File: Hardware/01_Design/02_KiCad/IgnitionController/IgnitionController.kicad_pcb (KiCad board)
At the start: 2 copper layers, 179 parts, among them J1 770669-1, Q1 SS8050, Q10 IRF540N, Q11 IRF540N, Q2 DMP6050SSD, Q3 DMP6050SSD, Q4 RSJ250P10, Q5 BC856, Q6 IRF9Z34NSPbF, Q7 SS8050, Q8 IRF540N, Q9 IRF540N, U1 ATmega328PB-A, U10 TLV2372, U11 TLV2372, U12 STM32F407VGTx, U14 AT24CS01-SSHM, U15 MCP2557FD-xSN, U19 IXDN602, U2 4N35, U20 IXDN602, U23 4N35, U24 4N35, U25 TXS0104EPW, U3 LM2575-3.3BU, U4 LM2575-5.0BU, U5 4N35, U6 4N35, U7 4N35, U8 TXS0104EPW, U9 LM2575-5.0BU, Y1 16MHz, Y2 32.768kHz, Y3 8MHz

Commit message: Initial routing of Power supply
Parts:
- removed C10, C8: UCL1V331MNL1GS, Capacitor_SMD:CP_Elec_10x12.5
- removed C6: UCL1V101MNL1GS, Capacitor_SMD:CP_Elec_8x11.9
- removed D11: RED, LED_SMD:LED_0805_2012Metric_Pad1.15x1.40mm_HandSolder
- removed D9: SS14, Diode_SMD:D_SMA
- removed L3, L4: L_Iron, Inductor_SMD:L_7.3x7.3_H3.5
- removed R11: 470R, Resistor_SMD:R_0805_2012Metric_Pad1.20x1.40mm_HandSolder
- added C43: 1u, Capacitor_SMD:C_0603_1608Metric_Pad1.08x0.95mm_HandSolder, F.Cu at (169.6, 36.0)
- added C44: 0.1u, Capacitor_SMD:C_0603_1608Metric_Pad1.08x0.95mm_HandSolder, F.Cu at (169.6, 38.5)
- added C45: 100n, Capacitor_SMD:C_0603_1608Metric_Pad1.08x0.95mm_HandSolder, F.Cu at (169.6, 41.0)
- added C46: 100n, Capacitor_SMD:C_0603_1608Metric_Pad1.08x0.95mm_HandSolder, F.Cu at (169.6, 43.5)
- added C47: 0.1u, Capacitor_SMD:C_0603_1608Metric_Pad1.08x0.95mm_HandSolder, F.Cu at (174.0, 20.9)
- added C48: 1u, Capacitor_SMD:C_0603_1608Metric_Pad1.08x0.95mm_HandSolder, F.Cu at (174.0, 23.4)
- added C49: 1u, Capacitor_SMD:C_0603_1608Metric_Pad1.08x0.95mm_HandSolder, F.Cu at (174.0, 26.0)
- added C50: 0.1u, Capacitor_SMD:C_0603_1608Metric_Pad1.08x0.95mm_HandSolder, F.Cu at (174.0, 28.5)
- added C51: 0.1u, Capacitor_SMD:C_0603_1608Metric_Pad1.08x0.95mm_HandSolder, F.Cu at (174.0, 31.0)
- added C52: UCL1V101MNL1GS, Capacitor_SMD:CP_Elec_8x11.9, F.Cu at (76.7, 98.0)
- added C53: UCL0J331MCL1GS, Capacitor_SMD:CP_Elec_6.3x7.7, F.Cu at (76.4, 108.4)
- added C54: UCL0J331MCL1GS, Capacitor_SMD:CP_Elec_6.3x7.7, F.Cu at (76.5, 85.6)
- added D23: SM6T100A, Diode_SMD:D_SMB, F.Cu at (271.6, 78.0)
- added D24: SM6T100A, Diode_SMD:D_SMB, F.Cu at (271.6, 83.6)
- added D25: SM6T100A, Diode_SMD:D_SMB, F.Cu at (271.6, 89.1)
- added D26: SM6T100A, Diode_SMD:D_SMB, F.Cu at (271.6, 94.7)
- added D27: RED, LED_SMD:LED_1206_3216Metric_Pad1.42x1.75mm_HandSolder, F.Cu at (206.0, 62.7)
- added D28: RED, LED_SMD:LED_1206_3216Metric_Pad1.42x1.75mm_HandSolder, F.Cu at (206.0, 66.1)
- added D29: RED, LED_SMD:LED_1206_3216Metric_Pad1.42x1.75mm_HandSolder, F.Cu at (206.0, 69.5)
- added D30: RED, LED_SMD:LED_1206_3216Metric_Pad1.42x1.75mm_HandSolder, F.Cu at (206.0, 72.9)
- added D31: SS14, Diode_SMD:D_SMA, B.Cu at (90.6, 107.6)
- added D32: RED, LED_SMD:LED_0805_2012Metric_Pad1.15x1.40mm_HandSolder, F.Cu at (100.8, 98.2)
- added J2: Conn_02x03_Odd_Even, Connector_IDC:IDC-Header_2x03_P2.54mm_Vertical, F.Cu at (223.2, 94.5)
- added J3: FTSH-105-01-L-DV-A, FTSH-105-01-L-DV-A:FTSH-105-XX-YYY-DV-A, F.Cu at (234.8, 93.3)
- added L6: SRR1280-331K, Inductor_SMD:L_Bourns_SRR1260, F.Cu at (91.0, 103.4)
- added L7: SRR1280-331K, Inductor_SMD:L_Bourns_SRR1260, F.Cu at (91.0, 87.6)
- added Q12: IRF540N, Package_TO_SOT_THT:TO-220-3_Vertical, F.Cu at (259.0, 79.2)
- added Q13: IRF540N, Package_TO_SOT_THT:TO-220-3_Vertical, F.Cu at (259.0, 85.1)
- added Q14: IRF540N, Package_TO_SOT_THT:TO-220-3_Vertical, F.Cu at (259.0, 91.1)
- added Q15: IRF540N, Package_TO_SOT_THT:TO-220-3_Vertical, F.Cu at (259.0, 97.1)
- added R58: 120R, Resistor_SMD:R_0603_1608Metric_Pad0.98x0.95mm_HandSolder, F.Cu at (178.3, 36.0)
- added R66: 100R, Resistor_SMD:R_0603_1608Metric_Pad0.98x0.95mm_HandSolder, F.Cu at (277.9, 76.5)
- added R67: 100R, Resistor_SMD:R_0603_1608Metric_Pad0.98x0.95mm_HandSolder, F.Cu at (277.9, 79.0)
- added R68: 100R, Resistor_SMD:R_0603_1608Metric_Pad0.98x0.95mm_HandSolder, F.Cu at (277.9, 81.5)
- added R69: 100R, Resistor_SMD:R_0603_1608Metric_Pad0.98x0.95mm_HandSolder, F.Cu at (277.9, 84.0)
- added R70: 7K, Resistor_SMD:R_0603_1608Metric_Pad0.98x0.95mm_HandSolder, F.Cu at (182.7, 28.5)
- added R71: 10K, Resistor_SMD:R_0603_1608Metric_Pad0.98x0.95mm_HandSolder, F.Cu at (182.7, 31.0)
- added R72: 8.2K, Resistor_SMD:R_0603_1608Metric_Pad0.98x0.95mm_HandSolder, F.Cu at (182.7, 33.5)
- added R73: 8.2K, Resistor_SMD:R_0603_1608Metric_Pad0.98x0.95mm_HandSolder, F.Cu at (182.7, 36.0)
- added R74: 7K, Resistor_SMD:R_0603_1608Metric_Pad0.98x0.95mm_HandSolder, F.Cu at (182.7, 38.5)
- added R75: 10K, Resistor_SMD:R_0603_1608Metric_Pad0.98x0.95mm_HandSolder, F.Cu at (182.7, 41.0)
- added R76: 10K, Resistor_SMD:R_0603_1608Metric_Pad0.98x0.95mm_HandSolder, F.Cu at (182.7, 43.5)
- added R77: 100R, Resistor_SMD:R_0603_1608Metric_Pad0.98x0.95mm_HandSolder, F.Cu at (189.0, 23.2)
- added R78: 100R, Resistor_SMD:R_0603_1608Metric_Pad0.98x0.95mm_HandSolder, F.Cu at (189.0, 25.7)
- added R79: 100R, Resistor_SMD:R_0603_1608Metric_Pad0.98x0.95mm_HandSolder, F.Cu at (189.0, 28.2)
- added R80: 100R, Resistor_SMD:R_0603_1608Metric_Pad0.98x0.95mm_HandSolder, F.Cu at (189.0, 30.7)
- added R81: 2K, Resistor_SMD:R_0603_1608Metric_Pad0.98x0.95mm_HandSolder, F.Cu at (189.0, 33.2)
- added R82: 2K, Resistor_SMD:R_0603_1608Metric_Pad0.98x0.95mm_HandSolder, F.Cu at (189.0, 35.7)
- added R83: 2K, Resistor_SMD:R_0603_1608Metric_Pad0.98x0.95mm_HandSolder, F.Cu at (189.0, 38.2)
- added R84: 2K, Resistor_SMD:R_0603_1608Metric_Pad0.98x0.95mm_HandSolder, F.Cu at (189.0, 40.7)
- added R85: 470R, Resistor_SMD:R_0603_1608Metric_Pad0.98x0.95mm_HandSolder, F.Cu at (104.3, 101.5)
- added U13: TLV2372, Package_SO:SOIC-8_5.3x6.2mm_P1.27mm, F.Cu at (208.2, 78.5)
- added U16: MAX232, Package_SO:SOIC-16_3.9x9.9mm_P1.27mm, F.Cu at (207.2, 55.3)
- added U21: IXDN602, Package_SO:SO-8_3.9x4.9mm_P1.27mm, F.Cu at (198.7, 79.1)
- added U22: IXDN602, Package_SO:SO-8_3.9x4.9mm_P1.27mm, F.Cu at (210.9, 101.7)
- C1, C13, C14, C15, C16, C17, C18, C19, C2, C20, C21, C22, C23, C24, C25, C26, C27, C28, C29, C3, C30, C31, C32, C33, C34, C35, C36, C37, C38, C39, C4, C40, C41, C42, C5, C7: footprint Capacitor_SMD:C_0805_2012Metric_Pad1.18x1.45mm_HandSolder -> Capacitor_SMD:C_0603_1608Metric_Pad1.08x0.95mm_HandSolder
- C12: value UCL1V331MNL1GS -> UCL0J331MCL1GS; footprint Capacitor_SMD:CP_Elec_10x12.5 -> Capacitor_SMD:CP_Elec_6.3x7.7
- D12, D13, D15, D8, Q5, U3, U4, U9: moved to B.Cu
- L5: value L_Iron -> SRR1280-331K; footprint Inductor_SMD:L_7.3x7.3_H3.5 -> Inductor_SMD:L_Bourns_SRR1260
- Q4: value RSJ250P10 -> RSJ250P10FRATL; footprint Package_TO_SOT_SMD:TO-263-2 -> Library:TO-263-2_Transistor; moved to B.Cu
- Q6: value IRF9Z34NSPbF -> 942-IRF9Z34NSPBF; footprint Package_TO_SOT_SMD:TO-263-2 -> Library:TO-263-2_Transistor; moved to B.Cu
- R1, R10, R12, R13, R14, R2, R3, R4, R40, R41, R42, R43, R44, R45, R46, R47, R48, R49, R50, R51, R52, R53, R54, R55, R56, R57, R59, R60, R61, R62, R63, R64, R65, R8: footprint Resistor_SMD:R_0805_2012Metric_Pad1.20x1.40mm_HandSolder -> Resistor_SMD:R_0603_1608Metric_Pad0.98x0.95mm_HandSolder
- R15, R16, R17, R18, R19, R20, R21, R22, R24, R25, R26, R27, R28, R29, R30, R31, R32, R33, R34, R35, R36, R37, R38, R39, R5, R6, R7: footprint Resistor_SMD:R_0805_2012Metric_Pad1.20x1.40mm_HandSolder -> Resistor_SMD:R_0603_1608Metric_Pad0.98x0.95mm_HandSolder; moved to F.Cu
- R23, R9: footprint Resistor_SMD:R_0815_2038Metric_Pad1.20x4.05mm_HandSolder -> Resistor_SMD:R_0603_1608Metric_Pad0.98x0.95mm_HandSolder
- U23, U24: moved to F.Cu
- moved U11 163.7 mm to (251.8, 23.7), turned to 0 degrees
- moved U10 162.9 mm to (251.8, 16.0), turned to 0 degrees
- moved U1 155.7 mm to (262.8, 30.3)
- moved R9 151.2 mm to (121.5, 116.4), turned to 90 degrees
- moved D8 151.1 mm to (98.5, 123.2)
- moved R33 145.8 mm to (244.4, 18.4), turned to 0 degrees
- moved R32 145.6 mm to (244.4, 15.8), turned to 0 degrees
- moved D16 145.4 mm to (100.8, 114.7)
- moved R31 145.3 mm to (244.4, 13.3), turned to 0 degrees
- moved D10 144.6 mm to (113.9, 108.9), turned to -90 degrees
- moved Q5 143.5 mm to (103.1, 123.2), turned to 180 degrees
- moved D14 142.2 mm to (100.8, 83.0)
- moved C7 141.7 mm to (124.4, 120.9), turned to 90 degrees
- moved R39 141.7 mm to (244.4, 33.4), turned to 0 degrees
- moved R38 141.5 mm to (244.4, 30.9), turned to 0 degrees
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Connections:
- net Net-(U1-PB3) renamed PMIC_SPI_MOSI
- net Net-(U1-PB4) renamed PMIC_SPI_MISO
- net Net-(U1-PB5) renamed PMIC_SPI_SCK
- net Net-(U12-NRST) renamed MCU_NRST
- J1 pad 1: unconnected-(J1-Pad1) -> GND
- J1 pad 10: unconnected-(J1-Pad10) -> INJ_FUEL_3
- J1 pad 11: unconnected-(J1-Pad11) -> MAP_SENSOR_SIGNAL
- J1 pad 12: unconnected-(J1-Pad12) -> TPS_SIGNAL
- J1 pad 13: unconnected-(J1-Pad13) -> COOLANT_TEMP_ADC_SIGNAL
- J1 pad 14: unconnected-(J1-Pad14) -> VSEN
- J1 pad 15: unconnected-(J1-Pad15) -> GND
- J1 pad 16: unconnected-(J1-Pad16) -> SENSOR_2_SIGNAL
- J1 pad 17: unconnected-(J1-Pad17) -> CAN-L
- J1 pad 18: unconnected-(J1-Pad18) -> UART_TX
- J1 pad 19: unconnected-(J1-Pad19) -> GND
- J1 pad 2: unconnected-(J1-Pad2) -> +BATT
- J1 pad 20: unconnected-(J1-Pad20) -> IGN_COIL_2
- J1 pad 21: unconnected-(J1-Pad21) -> IGN_COIL_4
- J1 pad 22: unconnected-(J1-Pad22) -> INJ_FUEL_2
- J1 pad 23: unconnected-(J1-Pad23) -> INJ_FUEL_4
- J1 pad 3: unconnected-(J1-Pad3) -> KL15
- J1 pad 4: unconnected-(J1-Pad4) -> SENSOR_1_SIGNAL
- J1 pad 5: unconnected-(J1-Pad5) -> CAN-H
- J1 pad 6: unconnected-(J1-Pad6) -> UART_RX
- J1 pad 7: unconnected-(J1-Pad7) -> IGN_COIL_1
- J1 pad 8: unconnected-(J1-Pad8) -> IGN_COIL_3
- J1 pad 9: unconnected-(J1-Pad9) -> INJ_FUEL_1
- Q4 pad 1: Net-(Q4-D) -> Net-(D8-A)
- Q4 pad 2: Net-(D8-A) -> Net-(Q4-D)
- Q6 pad 1: VCC -> Net-(D12-A)
- Q6 pad 2: Net-(D12-A) -> VCC
- U1 pad 29: unconnected-(U1-~{RESET}/PC6-Pad29) -> PMIC_RESET
- U12 pad 15: unconnected-(U12-PC0-Pad15) -> TPS_ADC_SIGNAL
- U12 pad 16: unconnected-(U12-PC1-Pad16) -> MAP_SENSOR_ADC_SIGNAL
- U12 pad 17: unconnected-(U12-PC2-Pad17) -> COOLANT_TEMP_ADC_SIGNAL
- U12 pad 63: unconnected-(U12-PC6-Pad63) -> Cylinder1FuelOut_Pin
- U12 pad 64: unconnected-(U12-PC7-Pad64) -> Cylinder2FuelOut_Pin
- U12 pad 65: unconnected-(U12-PC8-Pad65) -> Cylinder3FuelOut_Pin
- U12 pad 66: unconnected-(U12-PC9-Pad66) -> Cylinder4FuelOut_Pin
- U15 pad 6: unconnected-(U15-CANL-Pad6) -> CAN-L
- U15 pad 7: unconnected-(U15-CANH-Pad7) -> CAN-H
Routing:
- net GND: track 0.00 -> 249.2 mm, vias 0 -> 14
- net VCC: track 0.00 -> 84.0 mm, vias 0 -> 6
- net Net-(D12-A): track 0.00 -> 48.9 mm, vias 0 -> 4
- net Net-(D8-A): track 0.00 -> 46.5 mm, vias 0 -> 4
- net VPMIC: track 0.00 -> 46.2 mm, vias 0 -> 4
- net VSEN: track 0.00 -> 44.0 mm, vias 0 -> 3
- net Net-(Q4-D): track 0.00 -> 39.6 mm, vias 0 -> 3
- net Net-(D12-K): track 0.00 -> 35.9 mm, vias 0 -> 2
- net VMCU: track 0.00 -> 35.6 mm, vias 0 -> 3
- net Net-(D10-K): track 0.00 -> 22.0 mm, vias 0 -> 2
- net Net-(D13-K): track 0.00 -> 19.6 mm, vias 0 -> 3
- net Net-(D31-K): track 0.00 -> 13.9 mm, vias 0 -> 1
- net Net-(D15-K): track 0.00 -> 13.7 mm, vias 0 -> 1
- net Net-(D10-A): track 0.00 -> 10.2 mm
- net +BATT: track 0.00 -> 6.74 mm
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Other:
- copper layers 2 -> 4
- rule pad_to_mask_clearance: 0 -> 0.04
- board text added: "Layers: Top - Input Signals Layer 1 - Ground Layer 2 - Power Bottom - Output Signals"

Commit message: Added Crystal to PMIC
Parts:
- added R86: 10k, Resistor_SMD:R_0603_1608Metric_Pad0.98x0.95mm_HandSolder, F.Cu at (128.6, 85.5)
- added Y4: NX2016SA-16MHZ-EXS00A-CS07826, Library:NX2016SA16MHZEXS00ACS07826, F.Cu at (114.1, 94.1)
- Q2, Q3, R24, R25, R26, R27, R29, R30, R31, R32: moved to B.Cu
- U2, U5, U6, U7: moved to F.Cu
- moved Q3 176.5 mm to (76.7, 67.0), turned to 180 degrees
- moved Q2 176.4 mm to (76.7, 59.6), turned to 180 degrees
- moved R31 161.7 mm to (123.8, 121.1), turned to -90 degrees
- moved R35 159.8 mm to (89.7, 63.8)
- moved R36 158.1 mm to (89.6, 58.1)
- moved R38 157.4 mm to (89.6, 59.6)
- moved R37 157.3 mm to (89.6, 56.6)
- moved R32 155.9 mm to (129.4, 121.1), turned to -90 degrees
- moved U10 153.3 mm to (137.6, 118.3), turned to 180 degrees
- moved U1 151.7 mm to (124.7, 93.0)
- moved R19 149.8 mm to (89.7, 61.7)
- moved R18 148.4 mm to (89.7, 52.6)
- moved R17 147.4 mm to (89.7, 43.3)
- moved R16 146.6 mm to (89.7, 34.1)
- moved R30 143.4 mm to (126.5, 121.1), turned to -90 degrees
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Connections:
- C14 pad 1: GND -> Net-(U1-XTAL2/PB7)
- C14 pad 2: Net-(U1-XTAL1/PB6) -> GND
- C15 pad 2: Net-(U1-XTAL2/PB7) -> Net-(U1-XTAL1/PB6)
- C7 pad 1: Net-(Q4-D) -> +BATT_FUSE
- F1 pad 2: Net-(Q4-D) -> +BATT_FUSE
- Q2 pad 1: +BATT -> +BATT_FUSE
- Q2 pad 3: +BATT -> KL15
- Q3 pad 3: VMCU -> VMCU_OUT
- Q3 pad 5: VMCU_OUT -> VMCU
- Q3 pad 6: VMCU_OUT -> VMCU
- Q4 pad 2: Net-(Q4-D) -> +BATT_FUSE
- R24 pad 1: +BATT -> +BATT_FUSE
- U2 pad 5: +BATT -> +BATT_FUSE
- U5 pad 5: +BATT -> KL15
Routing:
- net GND: track 249.2 -> 527.9 mm, vias 14 -> 31
- net KL15: track 0.00 -> 184.7 mm, vias 0 -> 4
- net VPMIC: track 46.2 -> 228.4 mm, vias 4 -> 11
- net +BATT_FUSE: track 0.00 -> 165.9 mm, vias 0 -> 6
- net VMCU: track 35.6 -> 196.1 mm, vias 3 -> 12
- net VSEN: track 44.0 -> 141.9 mm, vias 3 -> 8
- net Net-(R5-Pad2): track 0.00 -> 68.4 mm
- net Net-(R6-Pad2): track 0.00 -> 60.3 mm
- net Net-(R7-Pad2): track 0.00 -> 51.9 mm
- net Net-(Q2A-G1): track 0.00 -> 46.8 mm, vias 0 -> 3
- net Net-(R15-Pad2): track 0.00 -> 43.9 mm
- net PMIC_SPI_MOSI: track 0.00 -> 42.7 mm, vias 0 -> 2
- net Net-(U11A-+): track 0.00 -> 42.3 mm, vias 0 -> 3
- net Net-(Q4-D): track 39.6 -> 0.00 mm, vias 3 -> 0
- net PMIC_SPI_MISO: track 0.00 -> 36.4 mm, vias 0 -> 2
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
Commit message: MCU HW Initial Layout
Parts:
- added Y1: FL0800011Q, Library:FL0800011Q, F.Cu at (99.6, 48.2)
- added Y3: XT1312HHRXX32K76E, Library:XT1312HHRXX32K76E, F.Cu at (105.0, 47.4)
- moved C32 134.8 mm to (97.4, 33.3), turned to 90 degrees
- moved C24 133.7 mm to (94.1, 33.3), turned to 90 degrees
- moved C33 133.7 mm to (99.0, 33.3), turned to 90 degrees
- moved R4 133.7 mm to (99.6, 56.0)
- moved D3 133.3 mm to (111.0, 66.2)
- moved C34 132.8 mm to (100.7, 33.3), turned to 90 degrees
- moved C25 132.7 mm to (95.7, 33.3), turned to 90 degrees
- moved C26 127.0 mm to (102.3, 33.3), turned to 90 degrees
- moved D4 126.9 mm to (117.1, 66.2)
- moved TP12 126.8 mm to (114.6, 62.1)
- moved C27 126.1 mm to (104.0, 33.3), turned to 90 degrees
- moved C28 125.3 mm to (105.6, 33.3), turned to 90 degrees
- moved C29 124.6 mm to (107.3, 33.3), turned to 90 degrees
- moved C30 123.9 mm to (108.9, 33.3), turned to 90 degrees
- moved C18 122.8 mm to (99.6, 44.6)
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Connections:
- C18 pad 1: GND -> Net-(U12-PH0)
- C18 pad 2: Net-(U12-PH0) -> GND
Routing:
- net GND: track 527.9 -> 687.2 mm, vias 31 -> 45
- net VMCU_OUT: track 11.7 -> 137.7 mm, vias 1 -> 10
- net Net-(U12-PH0): track 0.00 -> 19.1 mm
- net Net-(U12-PH1): track 0.00 -> 16.5 mm
- net MCU_NRST: track 0.00 -> 12.3 mm
- net Cylinder4Out_Pin: track 0.00 -> 8.56 mm
- net Net-(U12-PC14): track 0.00 -> 7.61 mm
- net Net-(U12-PC15): track 0.00 -> 6.87 mm
- net Net-(U12-BOOT0): track 0.00 -> 6.81 mm
- net Signal2_Pin: track 0.00 -> 6.33 mm
- net Signal1_Pin: track 0.00 -> 5.76 mm
- net Cylinder3Out_Pin: track 0.00 -> 5.13 mm
- net Net-(U12-PD15): track 0.00 -> 4.80 mm
- net Cylinder2Out_Pin: track 0.00 -> 4.44 mm
- net Cylinder1Out_Pin: track 0.00 -> 3.87 mm
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
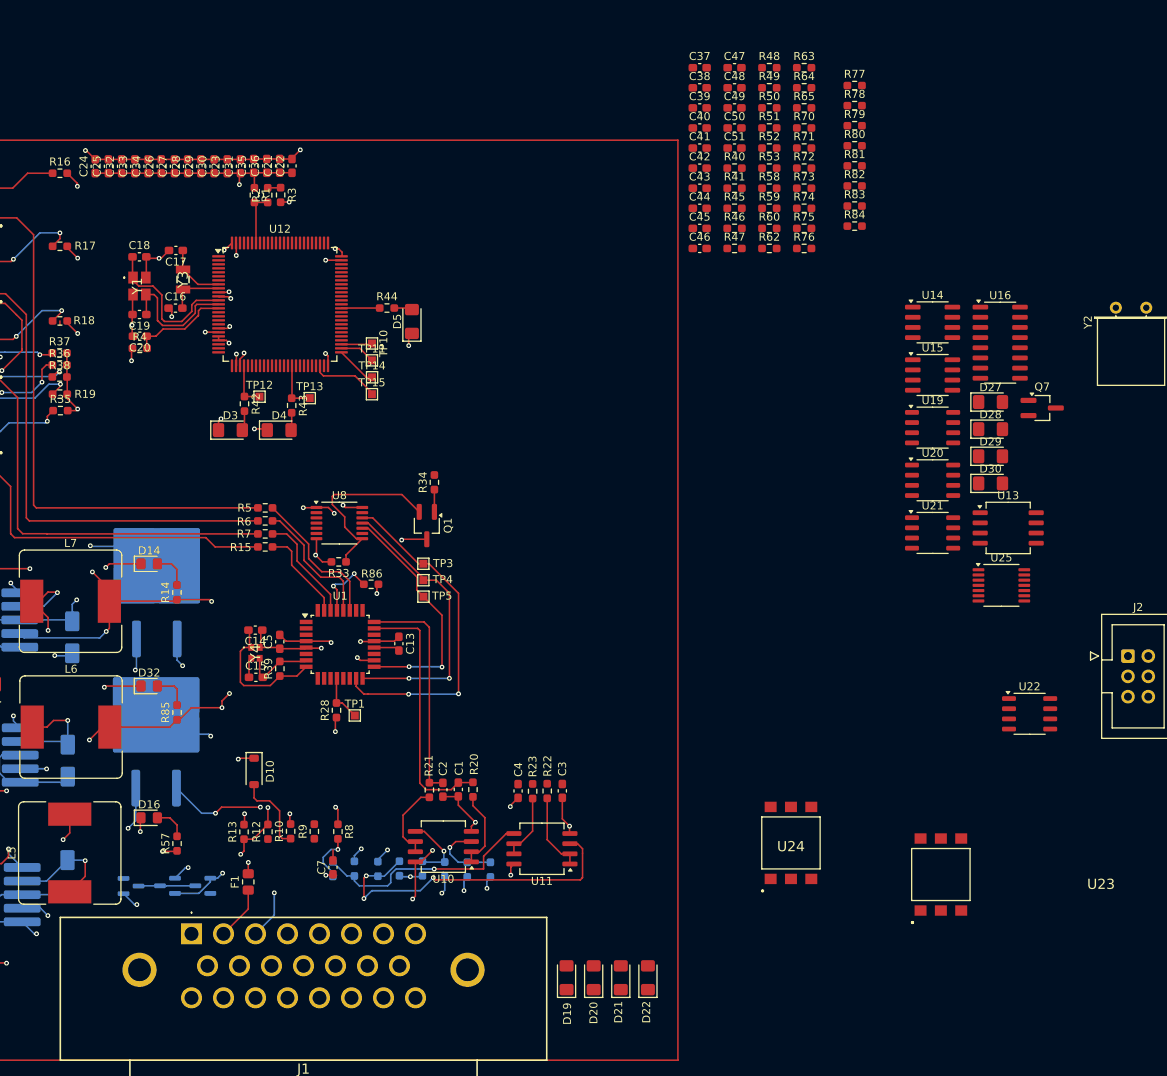
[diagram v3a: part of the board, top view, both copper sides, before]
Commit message: Added Peripheral HW Components
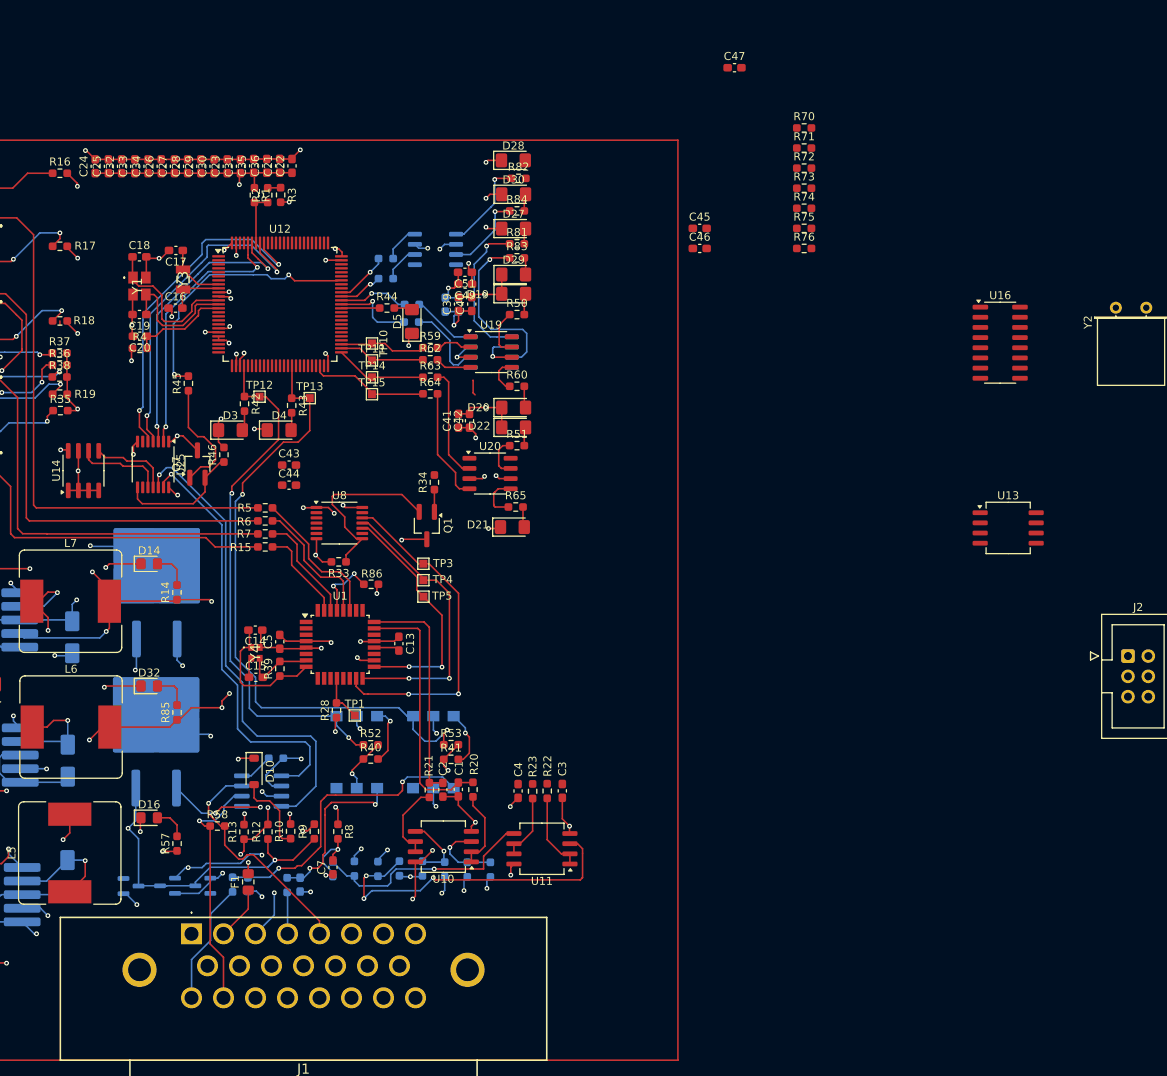
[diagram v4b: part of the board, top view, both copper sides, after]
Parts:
- C37, C38, C48, C50, R47, R48, R49, R77, R78, R79, R80, U15, U21, U22, U23, U24: moved to B.Cu
- moved R49 120.1 mm to (111.2, 123.0), turned to 90 degrees
- moved R48 118.6 mm to (118.0, 123.1), turned to 90 degrees
- moved C38 114.5 mm to (113.2, 123.0), turned to -90 degrees
- moved C37 113.7 mm to (119.7, 123.1), turned to -90 degrees
- moved U14 107.7 mm to (92.6, 71.3), turned to 90 degrees
- moved U25 107.1 mm to (101.3, 70.5), turned to -90 degrees
- moved Q7 105.8 mm to (106.8, 70.5), turned to 90 degrees
- moved R58 105.4 mm to (109.3, 115.7)
- moved U15 98.7 mm to (114.9, 111.4), turned to 180 degrees
- moved U22 94.3 mm to (136.6, 43.7)
- moved R52 89.7 mm to (128.5, 105.6)
- moved R40 86.7 mm to (128.5, 107.3)
- moved D19 85.7 mm to (146.4, 49.2), turned to 0 degrees
- moved R47 85.7 mm to (116.7, 107.2)
- moved R53 82.3 mm to (138.5, 105.6)
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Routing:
- net GND: track 687.2 -> 886.0 mm, vias 45 -> 63
- net KL30_OUT: track 18.2 -> 167.6 mm, vias 1 -> 7
- net VSEN_OUT: track 22.1 -> 113.5 mm, vias 3 -> 6
- net VMCU_OUT: track 137.7 -> 220.2 mm, vias 10 -> 13
- net Signal2_Pin: track 6.33 -> 79.8 mm, vias 0 -> 2
- net Signal1_Pin: track 5.76 -> 66.5 mm, vias 0 -> 2
- net Net-(U15-RXD): track 0.00 -> 60.3 mm, vias 0 -> 1
- net Net-(U15-TXD): track 0.00 -> 53.8 mm, vias 0 -> 1
- net I2C_SCL: track 0.00 -> 43.0 mm, vias 0 -> 2
- net I2C_SDA: track 0.00 -> 42.6 mm, vias 0 -> 2
- net Net-(C38-Pad1): track 0.00 -> 37.4 mm, vias 0 -> 2
- net CAN_RXD: track 0.00 -> 36.9 mm, vias 0 -> 2
- net CAN_TXD: track 0.00 -> 33.5 mm, vias 0 -> 2
- net OE_PIN2: track 0.00 -> 33.0 mm, vias 0 -> 2
- net CAN-L: track 0.00 -> 30.8 mm, vias 0 -> 1
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
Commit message: Routing PCB done
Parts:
- removed the Y1 at (260.7, 13.6)
- removed Y2: 32.768kHz, Crystal:Crystal_HC52-8mm_Horizontal
- removed the Y3 at (232.9, 50.9)
- C47, R70, R71, R74, R75, R76, U13: moved to B.Cu
- moved TP7 130.8 mm to (131.1, 113.3)
- moved R66 130.7 mm to (152.1, 41.0)
- moved R67 130.7 mm to (152.1, 43.5)
- moved R68 130.7 mm to (152.1, 46.0)
- moved R69 130.7 mm to (152.1, 48.5)
- moved R54 129.5 mm to (150.0, 71.0)
- moved R56 129.2 mm to (150.0, 73.5)
- moved R55 127.8 mm to (150.3, 58.4)
- moved R61 127.7 mm to (150.3, 55.8)
- moved D18 124.3 mm to (157.5, 118.2), turned to -90 degrees
- moved D17 122.4 mm to (157.4, 107.5), turned to -90 degrees
- moved D7 120.8 mm to (157.3, 96.8), turned to -90 degrees
- moved TP6 119.6 mm to (133.1, 107.1)
- moved J3 119.2 mm to (130.2, 36.3), turned to -90 degrees
- moved D6 119.0 mm to (157.3, 85.5), turned to -90 degrees
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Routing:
- net GND: track 886.0 -> 1096.0 mm, vias 63 -> 67
- net INJ_FUEL_1: track 0.00 -> 161.4 mm
- net COOLANT_TEMP_ADC_SIGNAL: track 0.00 -> 146.0 mm, vias 0 -> 2
- net INJ_FUEL_3: track 0.00 -> 130.9 mm
- net ADC_VMCU: track 0.00 -> 125.3 mm, vias 0 -> 5
- net INJ_FUEL_2: track 0.00 -> 121.5 mm, vias 0 -> 2
- net MAP_SENSOR_ADC_SIGNAL: track 0.00 -> 94.4 mm, vias 0 -> 2
- net TPS_ADC_SIGNAL: track 0.00 -> 92.0 mm, vias 0 -> 2
- net INJ_FUEL_4: track 0.00 -> 91.7 mm
- net ADC_VSENS: track 0.00 -> 91.5 mm, vias 0 -> 6
- net IGN_COIL_2: track 0.00 -> 76.4 mm, vias 0 -> 1
- net IGN_COIL_1: track 0.00 -> 74.9 mm
- net ADC_VBAT: track 32.3 -> 103.4 mm, vias 0 -> 2
- net IGN_COIL_4: track 0.00 -> 53.2 mm, vias 0 -> 1
- net MCU_SPI_CS: track 0.00 -> 51.4 mm, vias 0 -> 2
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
